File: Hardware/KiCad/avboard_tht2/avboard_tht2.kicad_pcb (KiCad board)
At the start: 4 copper layers, 177 x 152.1 mm, 139 parts, among them IC1 AS7C256C-15PCN, IC2_AUD0 74HC32, IC36 74HC4040, IC37 74HC30, IC39 74HC00, IC40 74HC4040, IC41 74HC00, IC43 74HC00, IC44 74HC86, IC45 74HC00, IC46 74HC257, IC47 74HC257, IC48 74HC564, IC4_AUD0 74HC00, IC53 74HC04, IC6_AUD0 74HC74, IC7_AUD0 LM358N, IC9 AS7C256C-15PCN, J1 5V, J2 5V, U1 W65C02S, U2 THS7374, U3 74VHC373, U4 74VHC373, U5 74VHC373, U8 74HC244, U9 74HC244

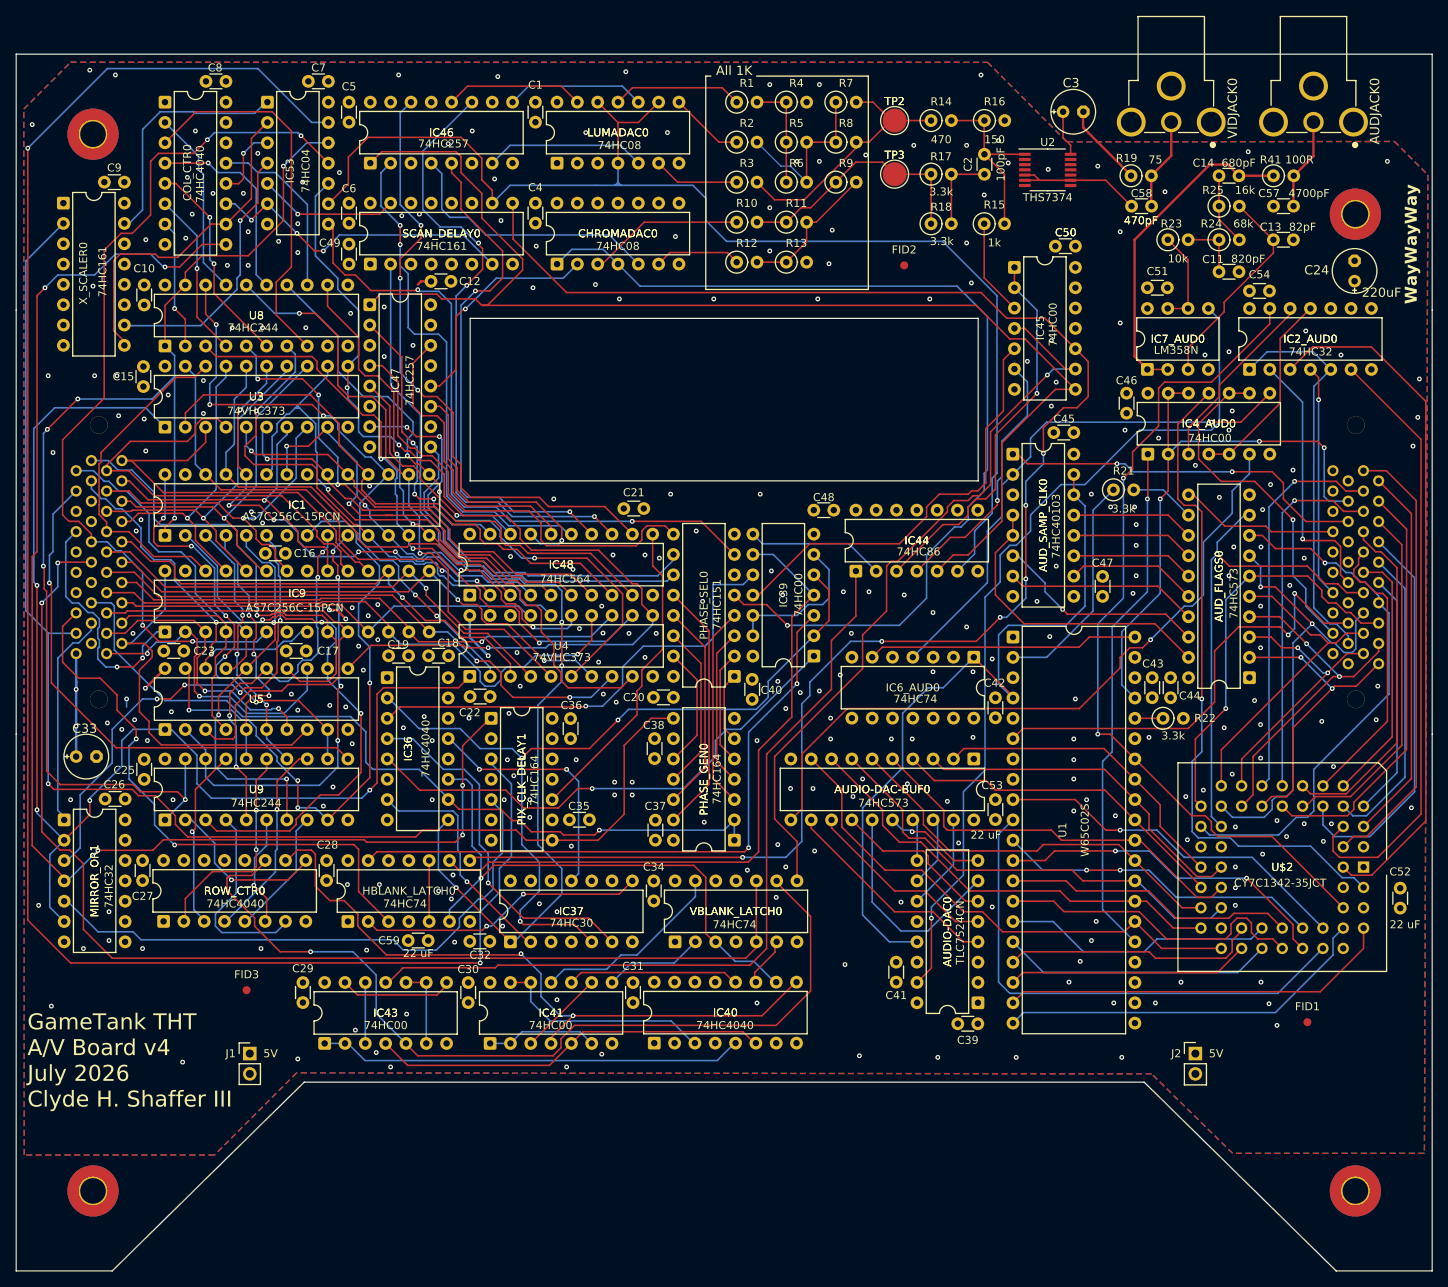
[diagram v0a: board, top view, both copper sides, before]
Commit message: fewer vias
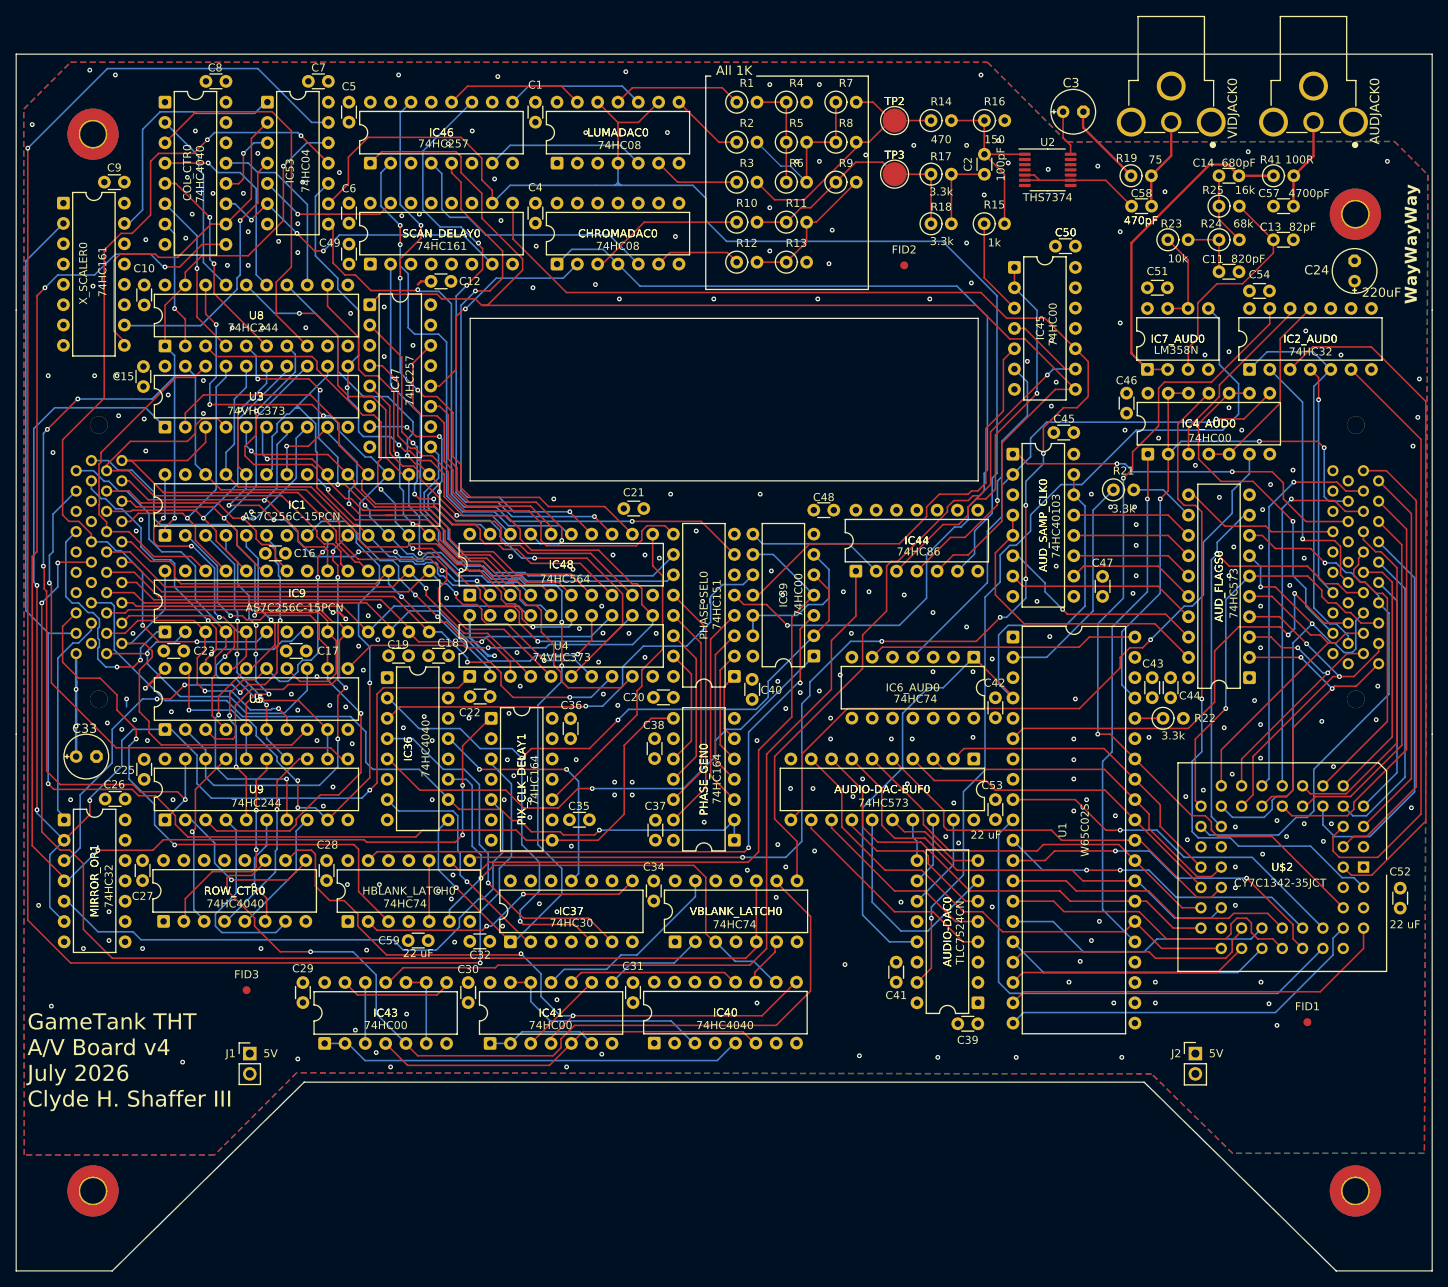
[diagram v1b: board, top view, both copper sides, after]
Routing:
- net Net-(AUDIO-DAC0-VREF): track 108.0 -> 110.8 mm
- net /Composite Video Generator/32H: track 58.3 -> 56.3 mm
- net Net-(IC7_AUD0A-+IN): track 26.6 -> 28.5 mm
- net VA5: track 72.8 -> 71.0 mm
- net /Audio Coprocessor/AD6: track 56.1 -> 57.9 mm
- net MA11: track 70.2 -> 68.6 mm, vias 3 -> 2
- net /Audio Coprocessor/AD5: track 56.6 -> 57.6 mm
- net MA1: track 73.5 -> 74.2 mm
- net MA9: track 32.8 -> 32.2 mm
- net VA8: track 28.4 -> 27.9 mm
- net Net-(PHASE_GEN0A-QE): track 15.3 -> 14.7 mm
- net VCC: track 48.2 -> 47.6 mm, vias 297 -> 298
- net /Audio Coprocessor/SysA7: track 45.5 -> 46.0 mm
- net VA11: track 38.9 -> 39.0 mm, vias 2 -> 1
- net Net-(AUDIO-DAC-BUF0A-4Q): vias 1 -> 0
